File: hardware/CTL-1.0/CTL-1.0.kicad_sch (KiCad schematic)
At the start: 58 parts, among them J1 Conn_02x16_Top_Bottom, J10 Conn_02x06_Odd_Even, J2 Conn_02x05_Odd_Even, J3 Conn_01x03, J4 Conn_01x02, J5 Conn_02x06_Odd_Even, J6 Conn_01x04, J7 Conn_01x04, J8 Conn_01x04, J9 Conn_01x06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

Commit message: modified:   .DS_Store 	modified:   README.md 	deleted:    hardware/CTL-1.0/CTL-1.0-backups/CTL-1.0-2025-05-23_140814.zip 	deleted:    hardware/CTL-1.0/CTL-1.0-backups/CTL-1.0-2025-05-23_142136.zip 	deleted:    hardware/CTL-1.0/CTL-1.0-backups/CTL-1.0-2025-05-23_145207.zip 	deleted:    hardware/CTL-1.0/CTL-1.0-backups/CTL-1.0-2025-05-23_145749.zip 	deleted:    hardware/CTL-1.0/CTL-1.0-backups/CTL-1.0-2025-06-03_185115.zip 	new file:   hardware/CTL-1.0/CTL-1.0-backups/CTL-1.0-2025-06-04_091843.zip 	new file:   hardware/CTL-1.0/CTL-1.0-backups/CTL-1.0-2025-06-04_105408.zip 	new file:   hardware/CTL-1.0/CTL-1.0-backups/CTL-1.0-2025-06-04_105918.zip 	new file:   hardware/CTL-1.0/CTL-1.0-backups/CTL-1.0-2025-06-04_110436.zip 	new file:   hardware/CTL-1.0/CTL-1.0-backups/CTL-1.0-2025-06-04_115049.zip 	new file:   hardware/CTL-1.0/CTL-1.0-backups/CTL-1.0-2025-06-04_132910.zip 	modified:   hardware/CTL-1.0/CTL-1.0.kicad_pcb 	modified:   hardware/CTL-1.0/CTL-1.0.kicad_prl 	modified:   hardware/CTL-1.0/CTL-1.0.kicad_sch 	new file:   hardware/PS-2.0/PS-2.0-backups/PS-2.0-2025-06-04_100004.zip 	new file:   hardware/PS-2.0/PS-2.0-backups/PS-2.0-2025-06-04_102434.zip 	new file:   hardware/PS-2.0/PS-2.0-backups/PS-2.0-2025-06-04_104734.zip 	new file:   hardware/PS-2.0/PS-2.0-backups/PS-2.0-2025-06-04_133345.zip 	modified:   hardware/PS-2.0/PS-2.0.kicad_pcb 	modified:   hardware/PS-2.0/PS-2.0.kicad_prl 	modified:   hardware/PS-2.0/PS-2.0.kicad_sch 	new file:   hardware/PS-2.0/~PS-2.0.kicad_pcb.lck 	new file:   hardware/PS-2.0/~PS-2.0.kicad_sch.lck 	modified:   pic/.DS_Store 	new file:   pic/PWM/Wave-pure-cut-driver-mosfet.png 	renamed:    pic/PWM/blend-cut-1/blend-cut-1-10.csv -> pic/PWM/blend-cut-1/CTL/blend-cut-1-10.csv 	renamed:    pic/PWM/blend-cut-1/blend-cut-1-10.png -> pic/PWM/blend-cut-1/CTL/blend-cut-1-10.png 	renamed:    pic/PWM/blend-cut-1/blend-cut-1-100.csv -> pic/PWM/blend-cut-1/CTL/blend-cut-1-100.csv 	renamed:    pic/PWM/blend-cut-1/blend-cut-1-100.png -> pic/PWM/ble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
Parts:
- added J11: Conn_02x02_Odd_Even, Connector_PinHeader_2.54mm:PinHeader_2x02_P2.54mm_Vertical, symbol Connector_Generic:Conn_02x02_Odd_Even
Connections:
- net +12V: now also J11.2 (Pin_2)
- net +5V: now also J11.1 (Pin_1)
- net RLY-A: now also J11.3 (Pin_3), J11.4 (Pin_4)
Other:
- moved on the sheet: C1, C2, C3, C4, C5, C6, D1, D2, D3, D4, D5, D6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

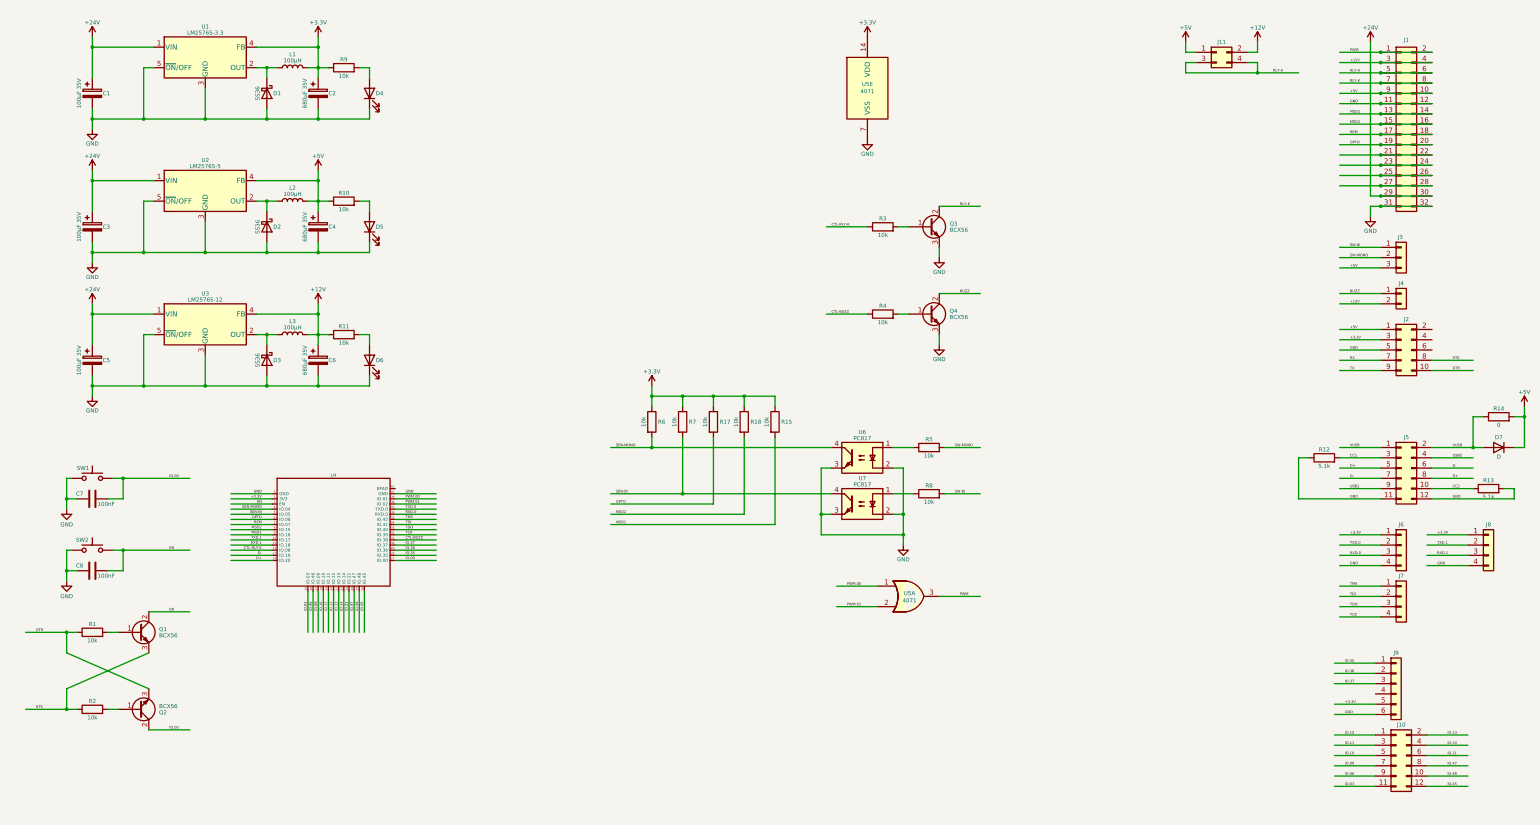
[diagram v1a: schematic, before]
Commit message: modified:   README.md 	deleted:    hardware/CTL-1.0/CTL-1.0-backups/CTL-1.0-2025-05-27_175205.zip 	deleted:    hardware/CTL-1.0/CTL-1.0-backups/CTL-1.0-2025-05-27_180035.zip 	deleted:    hardware/CTL-1.0/CTL-1.0-backups/CTL-1.0-2025-05-27_181441.zip 	deleted:    hardware/CTL-1.0/CTL-1.0-backups/CTL-1.0-2025-05-27_182529.zip 	deleted:    hardware/CTL-1.0/CTL-1.0-backups/CTL-1.0-2025-05-27_183819.zip 	deleted:    hardware/CTL-1.0/CTL-1.0-backups/CTL-1.0-2025-05-28_201558.zip 	deleted:    hardware/CTL-1.0/CTL-1.0-backups/CTL-1.0-2025-06-04_091843.zip 	new file:   hardware/CTL-1.0/CTL-1.0-backups/CTL-1.0-2025-06-05_141632.zip 	new file:   hardware/CTL-1.0/CTL-1.0-backups/CTL-1.0-2025-06-05_142549.zip 	new file:   hardware/CTL-1.0/CTL-1.0-backups/CTL-1.0-2025-06-05_143053.zip 	new file:   hardware/CTL-1.0/CTL-1.0-backups/CTL-1.0-2025-06-05_144242.zip 	new file:   hardware/CTL-1.0/CTL-1.0-backups/CTL-1.0-2025-06-05_144757.zip 	new file:   hardware/CTL-1.0/CTL-1.0-backups/CTL-1.0-2025-06-05_145506.zip 	modified:   hardware/CTL-1.0/CTL-1.0.kicad_pcb 	modified:   hardware/CTL-1.0/CTL-1.0.kicad_prl 	modified:   hardware/CTL-1.0/CTL-1.0.kicad_sch 	modified:   hardware/CTL-1.0/fp-info-cache 	new file:   hardware/PS-2.0/PS-2.0-backups/PS-2.0-2025-06-05_110653.zip 	new file:   hardware/PS-2.0/PS-2.0-backups/PS-2.0-2025-06-05_111332.zip 	new file:   hardware/PS-2.0/PS-2.0-backups/PS-2.0-2025-06-05_115228.zip 	new file:   hardware/PS-2.0/PS-2.0-backups/PS-2.0-2025-06-05_125334.zip 	modified:   hardware/PS-2.0/PS-2.0.kicad_pcb 	modified:   hardware/PS-2.0/PS-2.0.kicad_prl 	modified:   hardware/PS-2.0/PS-2.0.kicad_sch 	deleted:    hardware/PS-2.0/~PS-2.0.kicad_pcb.lck 	deleted:    hardware/PS-2.0/~PS-2.0.kicad_sch.lck 	modified:   pic/.DS_Store
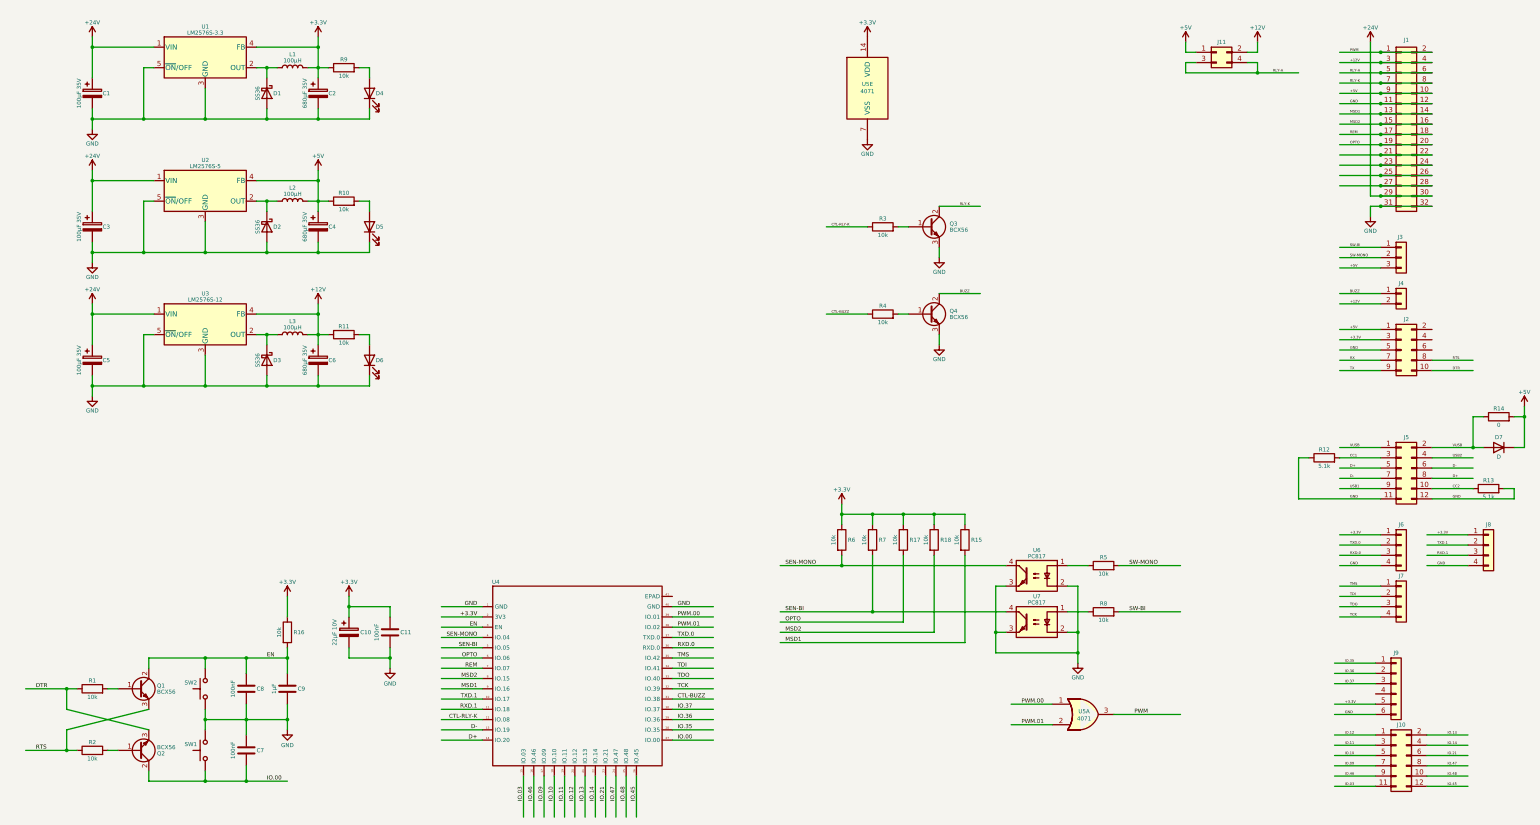
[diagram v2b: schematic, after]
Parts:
- added C10: 22µF 10V, Capacitor_Tantalum_SMD:CP_EIA-3528-12_Kemet-T_Pad1.50x2.35mm_HandSolder, symbol Device:C_Polarized
- added C11: 100nF, Capacitor_SMD:C_1206_3216Metric_Pad1.33x1.80mm_HandSolder, symbol Device:C
- added C9: 1µF, Capacitor_SMD:C_1206_3216Metric_Pad1.33x1.80mm_HandSolder, symbol Device:C
- added R16: 10k, Resistor_SMD:R_1206_3216Metric_Pad1.30x1.75mm_HandSolder, symbol Device:R
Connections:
- net +3.3V: now also C10.1, C11.2, R16.1
- net EN: now also C9.2, R16.2
- net GND: now also C10.2, C11.1, C9.1
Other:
- moved on the sheet: C8, Q1, Q2, R1, R15, R17, R18, R2, R5, R6, R7, R8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

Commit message: modified:   README.md 	new file:   firmware/.$Firmware-ESU-CTL-1.drawio.bkp 	new file:   firmware/.$Firmware-ESU-CTL-1.drawio.dtmp 	modified:   firmware/ESP32-S3 PWM/src/main.cpp 	new file:   firmware/Firmware-ESU-CTL-1.drawio 	new file:   hardware/CTL-1.0/#auto_saved_files# 	deleted:    hardware/CTL-1.0/CTL-1.0-backups/CTL-1.0-2025-05-30_180909.zip 	deleted:    hardware/CTL-1.0/CTL-1.0-backups/CTL-1.0-2025-06-03_190157.zip 	deleted:    hardware/CTL-1.0/CTL-1.0-backups/CTL-1.0-2025-06-03_222127.zip 	deleted:    hardware/CTL-1.0/CTL-1.0-backups/CTL-1.0-2025-06-03_222647.zip 	deleted:    hardware/CTL-1.0/CTL-1.0-backups/CTL-1.0-2025-06-03_223358.zip 	deleted:    hardware/CTL-1.0/CTL-1.0-backups/CTL-1.0-2025-06-03_223905.zip 	new file:   hardware/CTL-1.0/CTL-1.0-backups/CTL-1.0-2025-07-28_094555.zip 	new file:   hardware/CTL-1.0/CTL-1.0-backups/CTL-1.0-2025-07-28_104747.zip 	new file:   hardware/CTL-1.0/CTL-1.0-backups/CTL-1.0-2025-07-28_112613.zip 	new file:   hardware/CTL-1.0/CTL-1.0-backups/CTL-1.0-2025-07-28_114906.zip 	new file:   hardware/CTL-1.0/CTL-1.0-backups/CTL-1.0-2025-07-28_120848.zip 	renamed:    hardware/CTL-1.0/CTL-1.0-backups/CTL-1.0-2025-07-28_092533.zip -> hardware/CTL-1.0/CTL-1.0-backups/CTL-1.0-2025-07-29_085804.zip 	modified:   hardware/CTL-1.0/CTL-1.0.kicad_sch 	modified:   hardware/CTL-1.0/fp-info-cache 	deleted:    hardware/PS-2.0/PS-2.0-backups/PS-2.0-2025-06-05_125334.zip 	new file:   hardware/PS-2.0/PS-2.0-backups/PS-2.0-2025-07-28_120953.zip 	deleted:    hardware/XF-1.0/XF-1.0-backups/XF-1.0-2025-07-03_112321.zip 	new file:   hardware/XF-1.0/XF-1.0-backups/XF-1.0-2025-07-28_132022.zip
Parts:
- D7: value D -> BAT60A
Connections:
- net SEN-BI renamed SEN-COAG
- net SEN-MONO renamed SEN-CUT
- net SW-BI renamed SW-COAG
- net SW-MONO renamed SW-CUT
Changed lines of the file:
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@@
 		)
 	)
-	(label "SEN-BI"
+	(label "SEN-COAG"
 		(at 138.43 171.45 180)
 		(fields_autoplaced yes)
@@
 		)
 	)
-	(label "SW-BI"
+	(label "SW-COAG"
 		(at 299.72 162.56 0)
 		(fields_autoplaced yes)
@@
 		)
 	)
-	(label "SEN-BI"
+	(label "SEN-COAG"
 		(at 214.63 162.56 0)
 		(fields_autoplaced yes)
@@
 		)
 	)
-	(label "SW-BI"
+	(label "SW-COAG"
 		(at 354.33 72.39 0)
 		(fields_autoplaced yes)
@@
 		)
 	)
-	(label "SW-MONO"
+	(label "SW-CUT"
 		(at 299.72 151.13 0)
 		(fields_autoplaced yes)
@@
 		)
 	)
-	(label "SEN-MONO"
+	(label "SEN-CUT"
 		(at 214.63 151.13 0)
 		(fields_autoplaced yes)
@@
 		)
 	)
-	(label "SW-MONO"
+	(label "SW-CUT"
 		(at 354.33 74.93 0)
 		(fields_autoplaced yes)
@@
 		)
 	)
-	(label "SEN-MONO"
+	(label "SEN-CUT"
 		(at 138.43 168.91 180)
 		(fields_autoplaced yes)
@@
 			)
 		)
-		(property "Value" "D"
+		(property "Value" "BAT60A"
 			(at 391.16 124.206 0)
 			(effects

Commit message: deleted:    hardware/CTL-1.0/CTL-1.0-backups/CTL-1.0-2025-06-04_115049.zip 	deleted:    hardware/CTL-1.0/CTL-1.0-backups/CTL-1.0-2025-06-04_132910.zip 	deleted:    hardware/CTL-1.0/CTL-1.0-backups/CTL-1.0-2025-06-05_142549.zip 	deleted:    hardware/CTL-1.0/CTL-1.0-backups/CTL-1.0-2025-06-05_143053.zip 	deleted:    hardware/CTL-1.0/CTL-1.0-backups/CTL-1.0-2025-06-05_144242.zip 	new file:   hardware/CTL-1.0/CTL-1.0-backups/CTL-1.0-2025-08-01_111317.zip 	new file:   hardware/CTL-1.0/CTL-1.0-backups/CTL-1.0-2025-08-01_113544.zip 	new file:   hardware/CTL-1.0/CTL-1.0-backups/CTL-1.0-2025-08-01_114559.zip 	new file:   hardware/CTL-1.0/CTL-1.0-backups/CTL-1.0-2025-08-01_115359.zip 	new file:   hardware/CTL-1.0/CTL-1.0-backups/CTL-1.0-2025-08-01_115915.zip 	new file:   hardware/CTL-1.0/CTL-1.0-backups/CTL-1.0-2025-08-01_131607.zip 	modified:   hardware/CTL-1.0/CTL-1.0.kicad_pcb 	modified:   hardware/CTL-1.0/CTL-1.0.kicad_sch 	renamed:    hardware/CTL-1.0/CTL-1.0-backups/CTL-1.0-2025-06-05_144757.zip -> hardware/CTL-1.2/CTL-1.0-backups/CTL-1.0-2025-06-05_145506.zip 	new file:   hardware/CTL-1.2/CTL-1.0-backups/CTL-1.0-2025-06-10_100335.zip 	new file:   hardware/CTL-1.2/CTL-1.0-backups/CTL-1.0-2025-06-12_095314.zip 	new file:   hardware/CTL-1.2/CTL-1.0-backups/CTL-1.0-2025-07-03_115731.zip 	new file:   hardware/CTL-1.2/CTL-1.0-backups/CTL-1.0-2025-07-16_143147.zip 	new file:   hardware/CTL-1.2/CTL-1.0-backups/CTL-1.0-2025-07-24_151142.zip 	new file:   hardware/CTL-1.2/CTL-1.0-backups/CTL-1.0-2025-07-24_172002.zip 	new file:   hardware/CTL-1.2/CTL-1.0-backups/CTL-1.0-2025-07-25_175122.zip 	new file:   hardware/CTL-1.2/CTL-1.0-backups/CTL-1.0-2025-07-26_120011.zip 	new file:   hardware/CTL-1.2/CTL-1.0-backups/CTL-1.0-2025-07-26_120808.zip 	new file:   hardware/CTL-1.2/CTL-1.0-backups/CTL-1.0-2025-07-28_094555.zip 	new file:   hardware/CTL-1.2/CTL-1.0-backups/CTL-1.0-2025-07-28_104747.zip 	new file:   hardware/CTL-1.2/CTL-1.0-backups/CTL-1.0-2025-07-28_112613.zip 	new file:   ha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
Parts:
- added K1: G5V-1, Relay_THT:Relay_SPDT_Omron_G5V-1, symbol Relay:G5V-1
- added Q5: BCX56, Package_TO_SOT_SMD:SOT-89-3, symbol Transistor_BJT:BCX56
- added R19: 10k, Resistor_SMD:R_1206_3216Metric_Pad1.30x1.75mm_HandSolder, symbol Device:R
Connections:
- net GND: now also Q5.3 (E)
- new net: K1.2, Q5.2 (C)
- new net: K1.5, K1.6
- new net: Q5.1 (B), R19.2
